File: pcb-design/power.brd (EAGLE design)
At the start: 185.4 x 125.4 mm, 23 parts

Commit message: finished board
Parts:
- moved C1 5.00 mm to (55.9, 31.7)
- moved C10 5.00 mm to (156.2, 31.7)
- moved C11 5.00 mm to (146.1, 31.7)
- moved C12 5.00 mm to (137.2, 31.7)
- moved C2 5.00 mm to (41.9, 31.7)
- moved C3 5.00 mm to (31.8, 31.7)
- moved C4 5.00 mm to (22.9, 31.7)
- moved C5 5.00 mm to (113.0, 31.7)
- moved C6 5.00 mm to (99.1, 31.7)
- moved C7 5.00 mm to (88.9, 31.7)
- moved C8 5.00 mm to (80.0, 31.7)
- moved C9 5.00 mm to (170.2, 31.7)
- moved CONN1 5.00 mm to (171.4, 49.5)
- moved CONN2 5.00 mm to (171.4, 74.8)
- moved CV1 5.00 mm to (62.2, 102.8)
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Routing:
- net INPUT: track 726.1 -> 733.2 mm
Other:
- board size 185.4 x 125.4 mm -> 184.6 x 145.4 mm
- board text added: "BATTERY 11.1V"

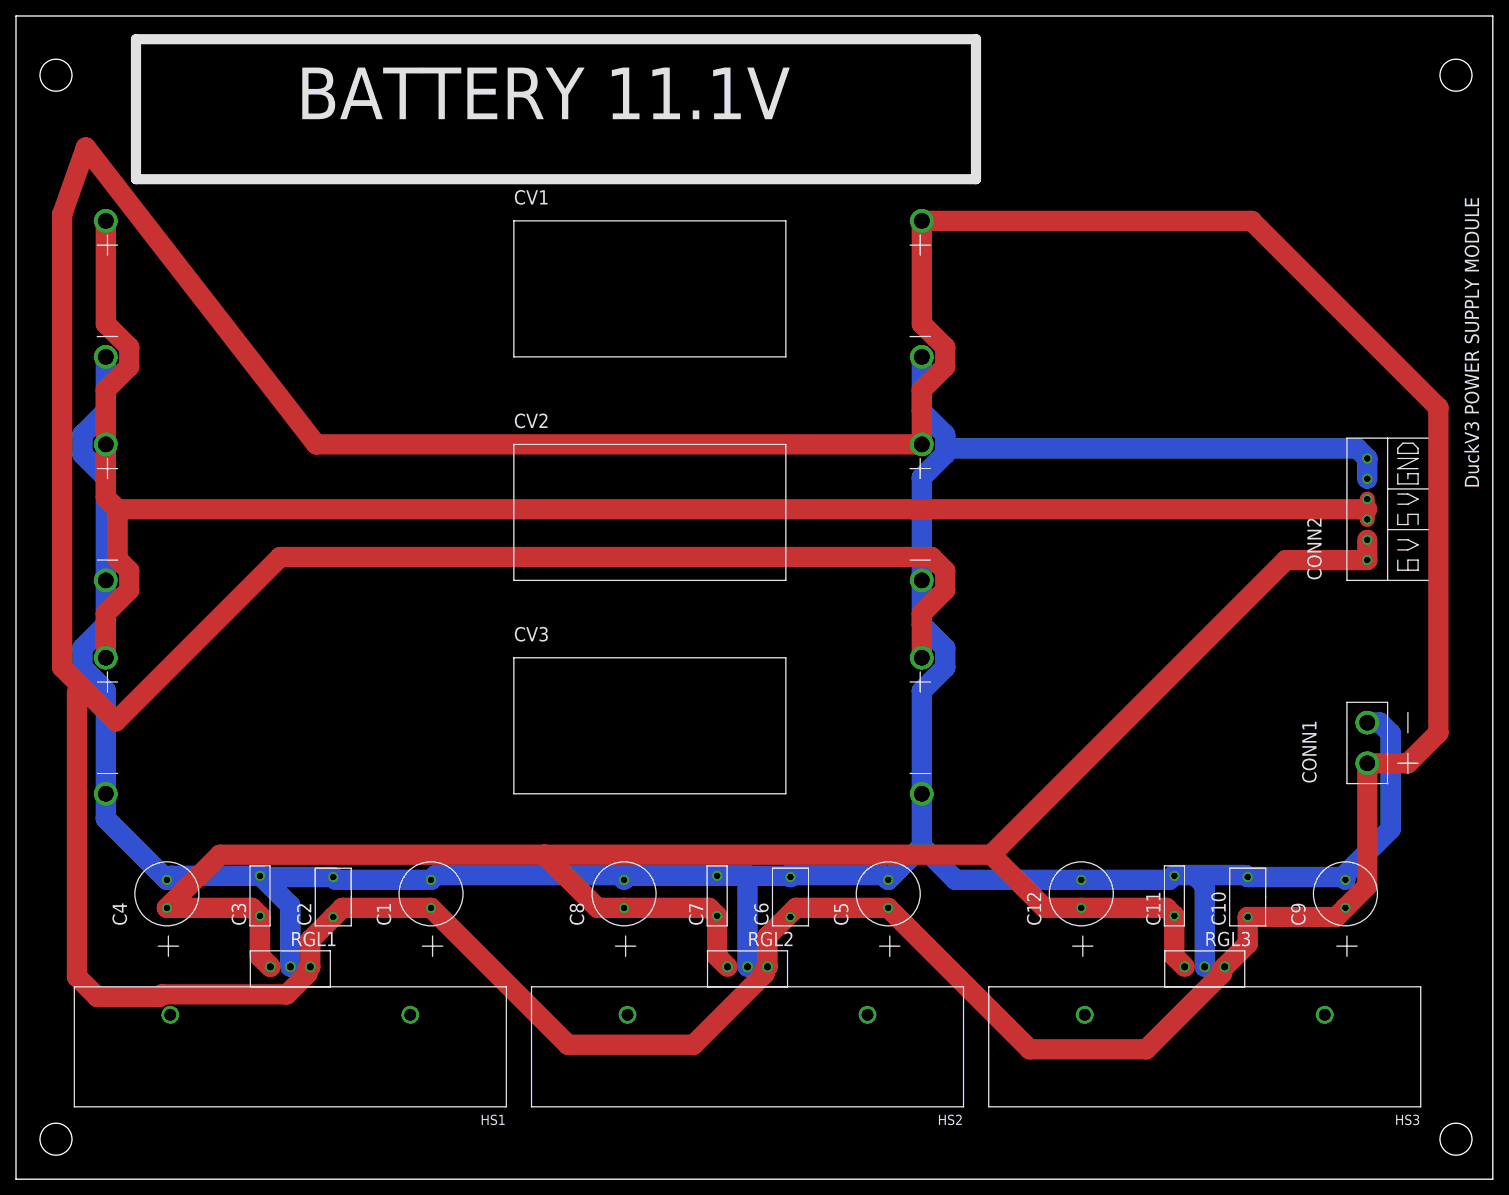
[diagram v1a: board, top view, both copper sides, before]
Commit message: wide battery place
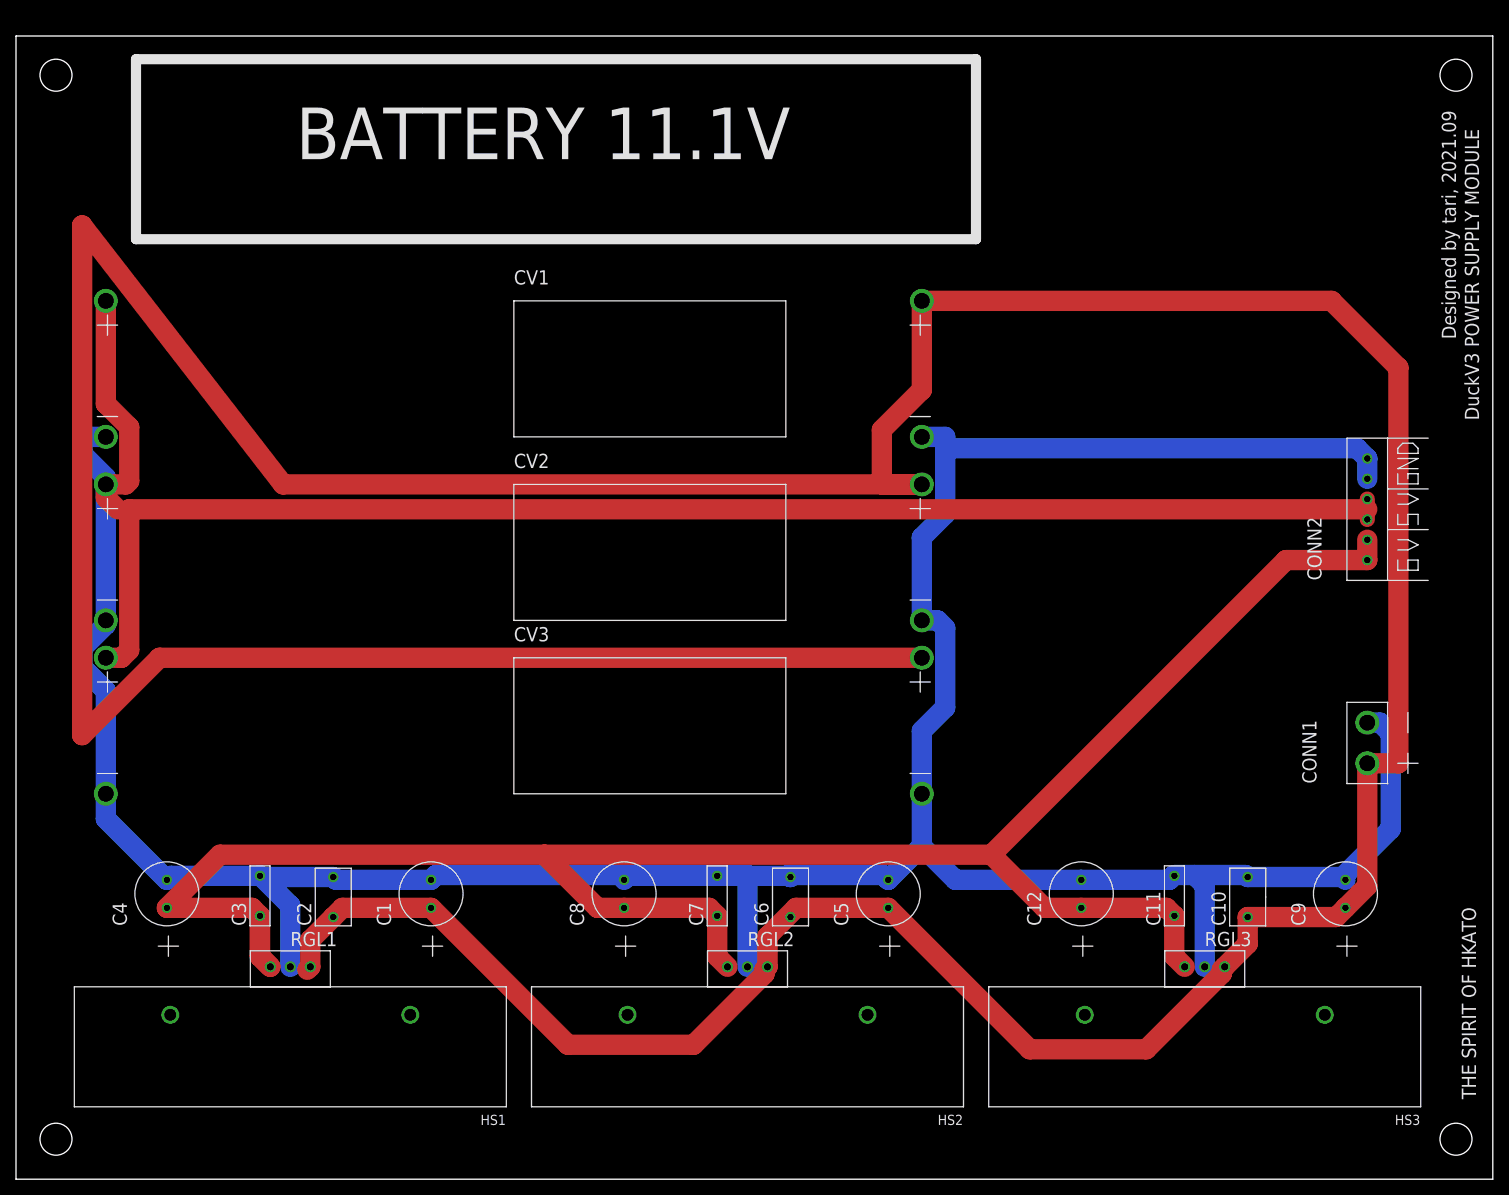
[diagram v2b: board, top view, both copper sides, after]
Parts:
- moved CV1 10.0 mm to (62.2, 92.8)
- moved CV2 5.00 mm to (62.2, 69.8)
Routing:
- net INPUT: track 733.2 -> 627.6 mm
- net GROUND: track 424.4 -> 409.0 mm
- net 5V: track 218.2 -> 208.8 mm
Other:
- board size 184.6 x 145.4 mm -> 184.6 x 142.9 mm
- board text added: "Designed by tari, 2021.09"
- board text added: "THE SPIRIT OF HKATO"

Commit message: Before dinner
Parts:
- added U$1, U$10, U$11, U$12, U$2, U$3, U$4, U$5, U$6, U$7, U$8, U$9: DIODE, library:DIODE
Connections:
- removed net 6V: C11.＋, C12.+, C3.＋, C4.+, C7.＋, C8.+, CONN2.6V0, CONN2.6V1, RGL1.OUTPUT, RGL2.OUTPUT, RGL3.OUTPUT
- new net N$1: C3.＋, C4.+, RGL1.OUTPUT, U$1.IN
- new net N$10: CONN2.5V0, CONN2.5V1, U$10.OUT, U$12.OUT, U$8.OUT
- new net N$11: CV1.IN-, CV1.OUT-, U$7.IN
- new net N$12: CV1.OUT+, U$8.IN
- new net N$13: CV2.OUT+, U$10.IN
- new net N$14: CONN2.6V0, CONN2.6V1, U$2.OUT, U$4.OUT, U$6.OUT
- new net N$2: C7.＋, C8.+, RGL2.OUTPUT, U$3.IN
- new net N$3: CV3.IN-, CV3.OUT-, U$11.IN
- new net N$4: CONN2.GND0, CONN2.GND1, U$1.OUT, U$3.OUT, U$5.OUT
- new net N$5: C10.-, C11.-, C12.-, C9.-, RGL3.GROUND, U$6.IN
- new net N$6: C5.-, C6.-, C7.-, C8.-, RGL2.GROUND, U$4.IN
- new net N$7: C1.-, C2.-, C3.-, C4.-, RGL1.GROUND, U$2.IN
- new net N$8: C11.＋, C12.+, RGL3.OUTPUT, U$5.IN
- new net N$9: CV2.IN-, CV2.OUT-, U$9.IN
- net 5V: now also U$12.IN; no longer CONN2.5V0, CONN2.5V1, CV1.OUT+, CV2.OUT+
- net GROUND: now also U$11.OUT, U$7.OUT, U$9.OUT; no longer C1.-, C10.-, C11.-, C12.-, C2.-, C3.-, C4.-, C5.-, C6.-, C7.-, C8.-, C9.-, CONN2.GND0, CONN2.GND1, CV1.IN-, CV1.OUT-, CV2.IN-, CV2.OUT-, CV3.IN-, CV3.OUT-, RGL1.GROUND, RGL2.GROUND, RGL3.GROUND
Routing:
- net GROUND: track 409.0 -> 23.9 mm
- net 6V: track 261.1 -> 0.00 mm
- net INPUT: track 627.6 -> 513.4 mm
- net N$5: track 0.00 -> 33.1 mm
- net 5V: track 208.8 -> 175.7 mm
- net N$3: track 0.00 -> 26.7 mm
- net N$1: track 0.00 -> 25.9 mm
- net N$8: track 0.00 -> 19.0 mm
- net N$2: track 0.00 -> 19.0 mm
- net N$13: track 0.00 -> 17.7 mm
- net N$4: track 0.00 -> 2.54 mm

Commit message: before lunch
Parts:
- renumbered U$1 to D1, U$10 to D10, U$11 to D11, U$12 to D12, U$2 to D2, U$3 to D3, U$4 to D4, U$5 to D5, U$6 to D6, U$7 to D7, U$8 to D8, U$9 to D9
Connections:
- removed net N$14: CONN2.6V0, CONN2.6V1, D2.OUT, D4.OUT, D6.OUT
- net GROUND: now also CONN2.GND0, CONN2.GND1, D2.OUT, D4.OUT, D6.OUT
- net N$4: now also CONN2.6V0, CONN2.6V1; no longer CONN2.GND0, CONN2.GND1
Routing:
- net N$4: track 2.54 -> 0.00 mm
- net GROUND: track 23.9 -> 26.5 mm

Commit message: Update board
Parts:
- moved D11 251.2 mm to (141.8, 101.6), turned to 90 degrees
- moved D12 230.7 mm to (142.2, 66.0), turned to 90 degrees
- moved D9 229.9 mm to (133.2, 101.6), turned to 90 degrees
- moved D10 209.4 mm to (133.3, 66.0), turned to 90 degrees
- moved D7 208.5 mm to (124.5, 101.6), turned to 90 degrees
- moved D6 198.7 mm to (142.2, 83.8), turned to 90 degrees
- moved D8 188.4 mm to (124.5, 66.0), turned to 90 degrees
- moved D4 178.4 mm to (133.3, 83.8), turned to 90 degrees
- moved D5 169.4 mm to (142.2, 48.3), turned to 90 degrees
- moved D1 107.1 mm to (124.5, 48.3), turned to 90 degrees
- moved D2 100.8 mm to (124.5, 83.8), turned to 90 degrees
- moved D3 68.6 mm to (133.3, 48.3), turned to 90 degrees
- moved CV3 19.2 mm to (62.2, 67.4), turned to 180 degrees
- moved CV2 19.1 mm to (62.2, 88.9), turned to 180 degrees
- moved CV1 17.6 mm to (62.2, 110.4), turned to 180 degrees
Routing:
- net INPUT: track 513.4 -> 292.8 mm
- net N$7: track 0.00 -> 164.8 mm
- net 5V: track 175.7 -> 41.7 mm
- net N$3: track 26.7 -> 160.5 mm
- net N$9: track 0.00 -> 131.4 mm
- net N$11: track 0.00 -> 115.6 mm
- net N$6: track 0.00 -> 113.7 mm
- net N$1: track 25.9 -> 130.5 mm
- net GROUND: track 26.5 -> 88.7 mm
- net N$2: track 19.0 -> 80.8 mm
- net N$5: track 33.1 -> 93.9 mm
- net N$4: track 0.00 -> 56.1 mm
- net N$10: track 0.00 -> 50.8 mm
- net N$12: track 0.00 -> 36.9 mm
- net N$8: track 19.0 -> 33.2 mm
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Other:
- board text removed: "Designed by tari, 2021.09"
- board text removed: "DuckV3 POWER SUPPLY MODULE"
- board text removed: "THE SPIRIT OF HKATO"

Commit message: correct err
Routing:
- net GROUND: track 88.7 -> 131.9 mm
- net INPUT: track 292.8 -> 286.2 mm
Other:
- board text added: "REMs DuckV3 Power Supply Unit"
- board text added: "THE SPIRIT OF HKATO"
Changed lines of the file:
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@@
 <hole x="180" y="138" drill="4"/>
 <wire x1="10.16" y1="114.3" x2="113.03" y2="114.3" width="1.27" layer="21"/>
-<text x="26.67" y="121.92" size="6.4516" layer="21">BATTERY 11.1V</text>
+<text x="95.25" y="128.27" size="6.4516" layer="21" rot="SR180">BATTERY 11.1V</text>
 <wire x1="10.16" y1="134.62" x2="113.03" y2="134.62" width="1.27" layer="25"/>
 <wire x1="10.16" y1="114.3" x2="10.16" y2="134.62" width="1.27" layer="25"/>
 <wire x1="113.03" y1="114.3" x2="113.03" y2="134.62" width="1.27" layer="25"/>
+<wire x1="166.37" y1="128.27" x2="166.37" y2="130.81" width="0.1524" layer="25"/>
+<wire x1="166.37" y1="130.81" x2="165.1" y2="130.81" width="0.1524" layer="25"/>
+<wire x1="165.1" y1="130.81" x2="162.56" y2="130.81" width="0.1524" layer="25"/>
+<wire x1="162.56" y1="130.81" x2="161.29" y2="130.81" width="0.1524" layer="25"/>
+<wire x1="161.29" y1="125.73" x2="162.56" y2="125.73" width="0.1524" layer="25"/>
+<wire x1="162.56" y1="125.73" x2="165.1" y2="125.73" width="0.1524" layer="25"/>
+<wire x1="165.1" y1="125.73" x2="166.37" y2="125.73" width="0.1524" layer="25"/>
+<wire x1="166.37" y1="125.73" x2="166.37" y2="128.27" width="0.1524" layer="25"/>
+<wire x1="166.37" y1="128.27" x2="168.91" y2="127" width="0.1524" layer="25"/>
+<wire x1="168.91" y1="127" x2="171.45" y2="125.73" width="0.1524" layer="25"/>
+<wire x1="171.45" y1="125.73" x2="171.45" y2="127" width="0.1524" layer="25"/>
+<wire x1="171.45" y1="127" x2="171.45" y2="129.54" width="0.1524" layer="25"/>
+<wire x1="171.45" y1="129.54" x2="171.45" y2="130.81" width="0.1524" layer="25"/>
+<wire x1="171.45" y1="130.81" x2="168.91" y2="129.54" width="0.1524" layer="25"/>
+<wire x1="166.37" y1="128.27" x2="168.91" y2="129.54" width="0.1524" layer="25"/>
+<wire x1="168.91" y1="129.54" x2="167.64" y2="132.08" width="0.1524" layer="25"/>
+<wire x1="166.37" y1="132.08" x2="167.64" y2="132.08" width="0.1524" layer="25"/>
+<wire x1="167.64" y1="133.35" x2="167.64" y2="132.08" width="0.1524" layer="25"/>
+<wire x1="167.64" y1="132.08" x2="166.37" y2="133.35" width="0.1524" layer="25"/>
+<wire x1="168.91" y1="127" x2="170.18" y2="124.46" width="0.1524" layer="25"/>
+<wire x1="170.18" y1="123.19" x2="170.18" y2="124.46" width="0.1524" layer="25"/>
+<wire x1="171.45" y1="123.19" x2="170.18" y2="124.46" width="0.1524" layer="25"/>
+<wire x1="170.18" y1="124.46" x2="171.45" y2="124.46" width="0.1524" layer="25"/>
+<wire x1="162.56" y1="127" x2="163.83" y2="127" width="0.1524" layer="25"/>
+<wire x1="162.56" y1="129.54" x2="163.83" y2="129.54" width="0.1524" layer="25"/>
+<wire x1="165.1" y1="127" x2="165.1" y2="129.54" width="0.1524" layer="25"/>
+<wire x1="171.45" y1="127" x2="176.53" y2="127" width="0.1524" layer="25"/>
+<wire x1="171.45" y1="129.54" x2="175.26" y2="129.54" width="0.1524" layer="25"/>
+<wire x1="175.26" y1="129.54" x2="173.99" y2="130.81" width="0.1524" layer="25"/>
+<wire x1="176.53" y1="127" x2="176.53" y2="125.73" width="0.1524" layer="25"/>
+<text x="181.61" y="8.89" size="1.778" layer="25" font="vector" rot="R90">THE SPIRIT OF HKATO</text>
+<text x="181.61" y="96.52" size="1.778" layer="25" font="vector" rot="R90">REMs DuckV3 Power Supply Unit</text>
+<wire x1="161.29" y1="125.73" x2="161.29" y2="128.27" width="0.1524" layer="25"/>
+<wire x1="161.29" y1="128.27" x2="161.29" y2="130.81" width="0.1524" layer="25"/>
+<wire x1="162.56" y1="130.81" x2="162.56" y2="133.35" width="0.1524" layer="25"/>
+<wire x1="162.56" y1="133.35" x2="165.1" y2="130.81" width="0.1524" layer="25"/>
+<wire x1="162.56" y1="125.73" x2="162.56" y2="123.19" width="0.1524" layer="25"/>
+<wire x1="162.56" y1="123.19" x2="165.1" y2="125.73" width="0.1524" layer="25"/>
+<wire x1="161.29" y1="128.27" x2="160.02" y2="128.27" width="0.1524" layer="25"/>
+<wire x1="160.02" y1="128.27" x2="158.75" y2="127" width="0.1524" layer="25"/>
+<wire x1="158.75" y1="127" x2="157.48" y2="128.27" width="0.1524" layer="25"/>
+<wire x1="157.48" y1="128.27" x2="158.75" y2="129.54" width="0.1524" layer="25"/>
+<wire x1="158.75" y1="129.54" x2="160.02" y2="128.27" width="0.1524" layer="25"/>
 </plain>
 <attributes>
@@
 <wire x1="39.66" y1="32.77" x2="39.66" y2="29.42" width="1.27" layer="1"/>
 <wire x1="39.66" y1="29.42" x2="36.79" y2="26.55" width="1.27" layer="1"/>
-<wire x1="168.91" y1="51.99" x2="163.9024" y2="56.9976" width="1.27" layer="1"/>
 <wire x1="36.79" y1="26.55" x2="33.1" y2="22.86" width="1.27" layer="1"/>
 <wire x1="11.43" y1="22.86" x2="11.23" y2="23.06" width="1.27" layer="1"/>
@@
 <wire x1="6.35" y1="90.17" x2="9.59" y2="93.41" width="1.27" layer="1"/>
 <wire x1="9.59" y1="93.41" x2="11.23" y2="93.41" width="1.27" layer="1"/>
-<wire x1="11.43" y1="72.39" x2="11.23" y2="93.41" width="0" layer="19" extent="1-1"/>
-<wire x1="6.35" y1="72.39" x2="6.35" y2="72.39" width="1.27" layer="1"/>
-<wire x1="6.35" y1="72.39" x2="11.43" y2="72.39" width="1.27" layer="1"/>
+<wire x1="11.43" y1="72.39" x2="6.35" y2="72.39" width="1.27" layer="1"/>
+<wire x1="11.23" y1="71.9" x2="11.43" y2="72.39" width="1.27" layer="1"/>
 </signal>
 <signal name="GROUND">
@@
 <wire x1="156.13" y1="102.87" x2="168.91" y2="90.09" width="1.27" layer="16"/>
 <wire x1="168.91" y1="90.09" x2="168.91" y2="87.55" width="1.27" layer="16"/>
-<wire x1="168.91" y1="87.55" x2="168.91" y2="57.07" width="0" layer="19" extent="1-1"/>
+<wire x1="168.91" y1="90.09" x2="163.83" y2="90.17" width="1.27" layer="16"/>
+<wire x1="163.83" y1="90.17" x2="163.83" y2="57.15" width="1.27" layer="16"/>
+<wire x1="168.91" y1="57.15" x2="163.83" y2="57.15" width="1.27" layer="16"/>
+<wire x1="168.91" y1="57.07" x2="168.91" y2="57.15" width="1.27" layer="16"/>
 </signal>
 <signal name="5V">
@@
 <contactref element="D12" pad="OUT"/>
 <wire x1="123.19" y1="76.2" x2="132.08" y2="76.2" width="1.27" layer="1"/>
-<wire x1="132.08" y1="76.2" x2="139.7" y2="76.2" width="1.27" layer="1"/>
-<wire x1="139.7" y1="76.2" x2="140.97" y2="76.2" width="1.27" layer="1"/>
+<wire x1="132.08" y1="76.2" x2="140.97" y2="76.2" width="1.27" layer="1"/>
 <wire x1="140.97" y1="76.2" x2="148.59" y2="76.2" width="1.27" layer="1"/>
 <wire x1="148.59" y1="76.2" x2="154.94" y2="82.55" width="1.27" layer="1"/>
 <wire x1="168.91" y1="82.55" x2="154.94" y2="82.55" width="1.27" layer="1"/>
 <wire x1="168.91" y1="85.01" x2="168.91" y2="82.55" width="1.27" layer="1"/>
-<wire x1="168.91" y1="85.01" x2="168.91" y2="82.47" width="0" layer="19" extent="1-1"/>
+<wire x1="168.91" y1="82.47" x2="168.91" y2="82.55" width="1.27" layer="1"/>
 </signal>
 <signal name="N$11">
